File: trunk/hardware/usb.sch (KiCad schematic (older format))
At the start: 9 parts, among them J1 USB-MINI-AB, U1 FT232-SSOP28

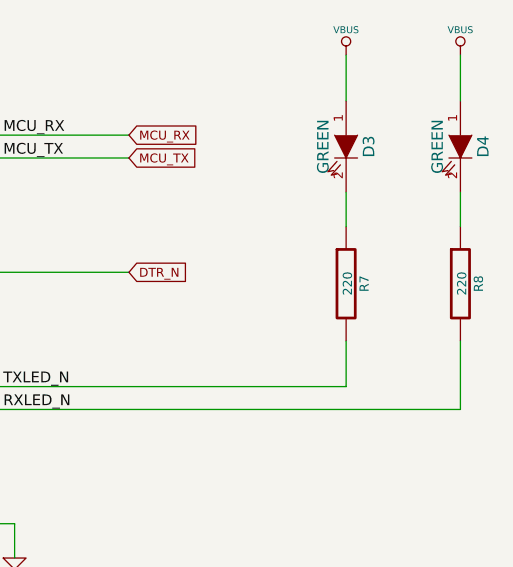
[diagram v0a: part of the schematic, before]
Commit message: Changed all 220ohm LED resistors to 1Kohm. This is how I actually built the first r116 test board. The LEDs are still too bright for my liking, actually. This way, we may also save a little battery power.
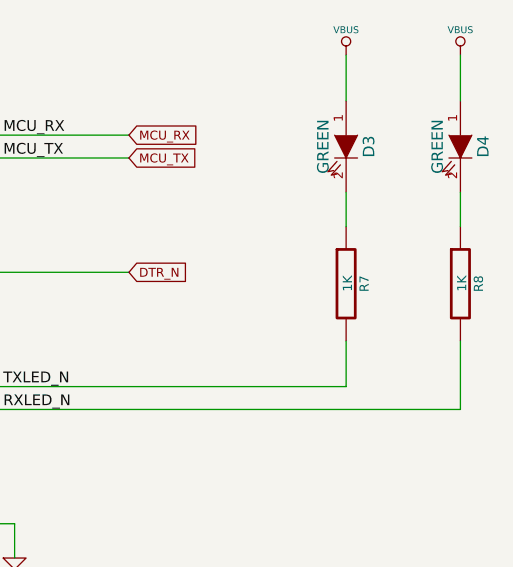
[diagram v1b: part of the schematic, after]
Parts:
- R7, R8: value 220 -> 1K
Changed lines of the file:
@@
 Sheet 3 6
 Title "FREAKDUINO-CHIBI 2.4GHz"
-Date "12 aug 2013"
+Date "13 aug 2013"
 Rev "v1.1"
 Comp "KiCAD version by Gruvin"
@@
 P 7900 3450
 F 0 "R7" V 7980 3450 40  0000 C CNN
-F 1 "220" V 7907 3451 40  0000 C CNN
+F 1 "1K" V 7907 3451 40  0000 C CNN
 F 2 "" V 7830 3450 30  0000 C CNN
 F 3 "" H 7900 3450 30  0000 C CNN
@@
 P 8400 3450
 F 0 "R8" V 8480 3450 40  0000 C CNN
-F 1 "220" V 8407 3451 40  0000 C CNN
+F 1 "1K" V 8407 3451 40  0000 C CNN
 F 2 "" V 8330 3450 30  0000 C CNN
 F 3 "" H 8400 3450 30  0000 C CNN
